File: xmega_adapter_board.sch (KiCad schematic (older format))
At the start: 15 parts, among them J1 Conn_01x04, J2 Conn_01x08, J3 Conn_01x08, J4 Conn_01x04, J5 Conn_01x08, J6 Conn_01x08, J7 Conn_01x08, J8 Conn_01x08, U1 ATxmega256D3-AU

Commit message: Schematic als PDF erstellt
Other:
- note added: "Stützkondensatoren, so dicht wie möglich an U1 platzieren!"
- moved on the sheet: C1, C2, C3, C4, C5, C6, J1, J2, J3, J4, J5, J6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

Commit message: Power LED als rote SMD LED hinzugefuegt
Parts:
- added D1: LED ROT (2,0V / 20mA), LED_SMD:LED_0805_2012Metric_Pad1.15x1.40mm_HandSolder, symbol Device:LED
- added R1: 68, Resistor_SMD:R_0805_2012Metric_Pad1.15x1.40mm_HandSolder, symbol Device:R
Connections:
- net GND: now also D1.1 (K)
- net VCC renamed +3V3
- net +3V3: now also R1.2
- new net: D1.2 (A), R1.1
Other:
- note added: "Spannungsversorgung"
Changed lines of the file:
@@
 Sheet 1 1
 Title "XMEGA Adapter Board "
-Date "2020-06-25"
-Rev "1.0.0"
+Date "2020-07-12"
+Rev "1.1.0"
 Comp ""
 Comment1 "Erstellt von: Thorsten Kattanek"
@@
 Wire Wire Line
 	2900 6300 2900 6500
-Text GLabel 2900 2500 1    50   Input ~ 0
+Text GLabel 700  1250 3    50   Input ~ 0
 VCC
 Text GLabel 3000 2500 1    50   Input ~ 0
@@
 Text Notes 7900 750  0    50   ~ 0
 Stützkondensatoren, so dicht wie möglich an U1 platzieren!
+$Comp
+L Device:LED D1
+U 1 1 5F0B2F15
+P 4300 1350
+F 0 "D1" H 4293 1095 50  0000 C CNN
+F 1 "LED ROT (2,0V / 20mA)" H 4293 1186 50  0000 C CNN
+F 2 "LED_SMD:LED_0805_2012Metric_Pad1.15x1.40mm_HandSolder" H 4300 1350 50  0001 C CNN
+F 3 "~" H 4300 1350 50  0001 C CNN
+	1    4300 1350
+	-1   0    0    1
+$EndComp
+Text GLabel 1100 1250 3    50   Input ~ 0
+GND
+Wire Wire Line
+	4450 1350 4650 1350
+$Comp
+L power:+3.3V #PWR01
+U 1 1 5F0BBD4E
+P 700 1000
+F 0 "#PWR01" H 700 850 50  0001 C CNN
+F 1 "+3.3V" H 715 1173 50  0000 C CNN
+F 2 "" H 700 1000 50  0001 C CNN
+F 3 "" H 700 1000 50  0001 C CNN
+	1    700  1000
+	1    0    0    -1
+$EndComp
+$Comp
+L power:GND #PWR03
+U 1 1 5F0BCF31
+P 1100 1000
+F 0 "#PWR03" H 1100 750 50  0001 C CNN
+F 1 "GND" H 1105 827 50  0000 C CNN
+F 2 "" H 1100 1000 50  0001 C CNN
+F 3 "" H 1100 1000 50  0001 C CNN
+	1    1100 1000
+	-1   0    0    1
+$EndComp
+Wire Wire Line
+	700  1000 700  1250
+Wire Wire Line
+	1100 1000 1100 1250
+Text Notes 600  650  0    50   ~ 0
+Spannungsversorgung
+Text GLabel 4650 1350 2    50   Input ~ 0
+GND
+Text GLabel 3100 1350 0    50   Input ~ 0
+VCC
+$Comp
+L Device:R R1
+U 1 1 5F101B02
+P 3550 1350
+F 0 "R1" V 3343 1350 50  0000 C CNN
+F 1 "68" V 3434 1350 50  0000 C CNN
+F 2 "Resistor_SMD:R_0805_2012Metric_Pad1.15x1.40mm_HandSolder" V 3480 1350 50  0001 C CNN
+F 3 "~" H 3550 1350 50  0001 C CNN
+	1    3550 1350
+	0    1    1    0
+$EndComp
+Wire Wire Line
+	3700 1350 4150 1350
+Wire Wire Line
+	3400 1350 3100 1350
+Text GLabel 2900 2500 1    50   Input ~ 0
+VCC
 $EndSCHEMATC

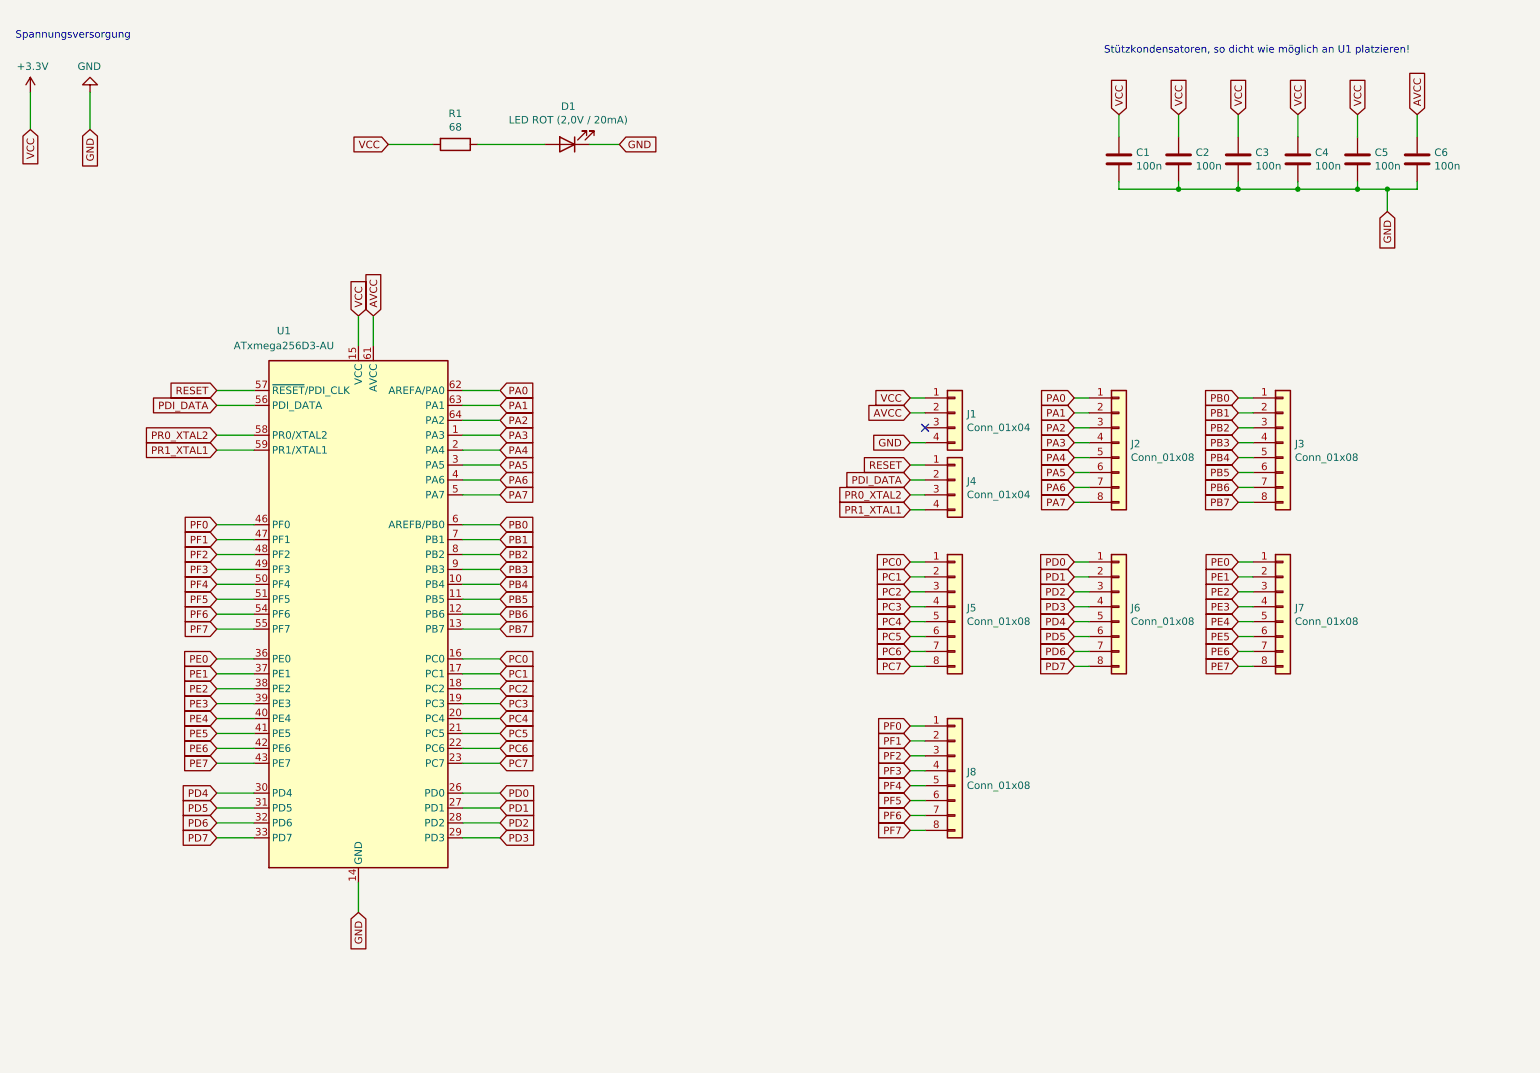
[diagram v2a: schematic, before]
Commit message: changed board to version 1.1.0 - added a 3.3 voltage regulator and a reset button
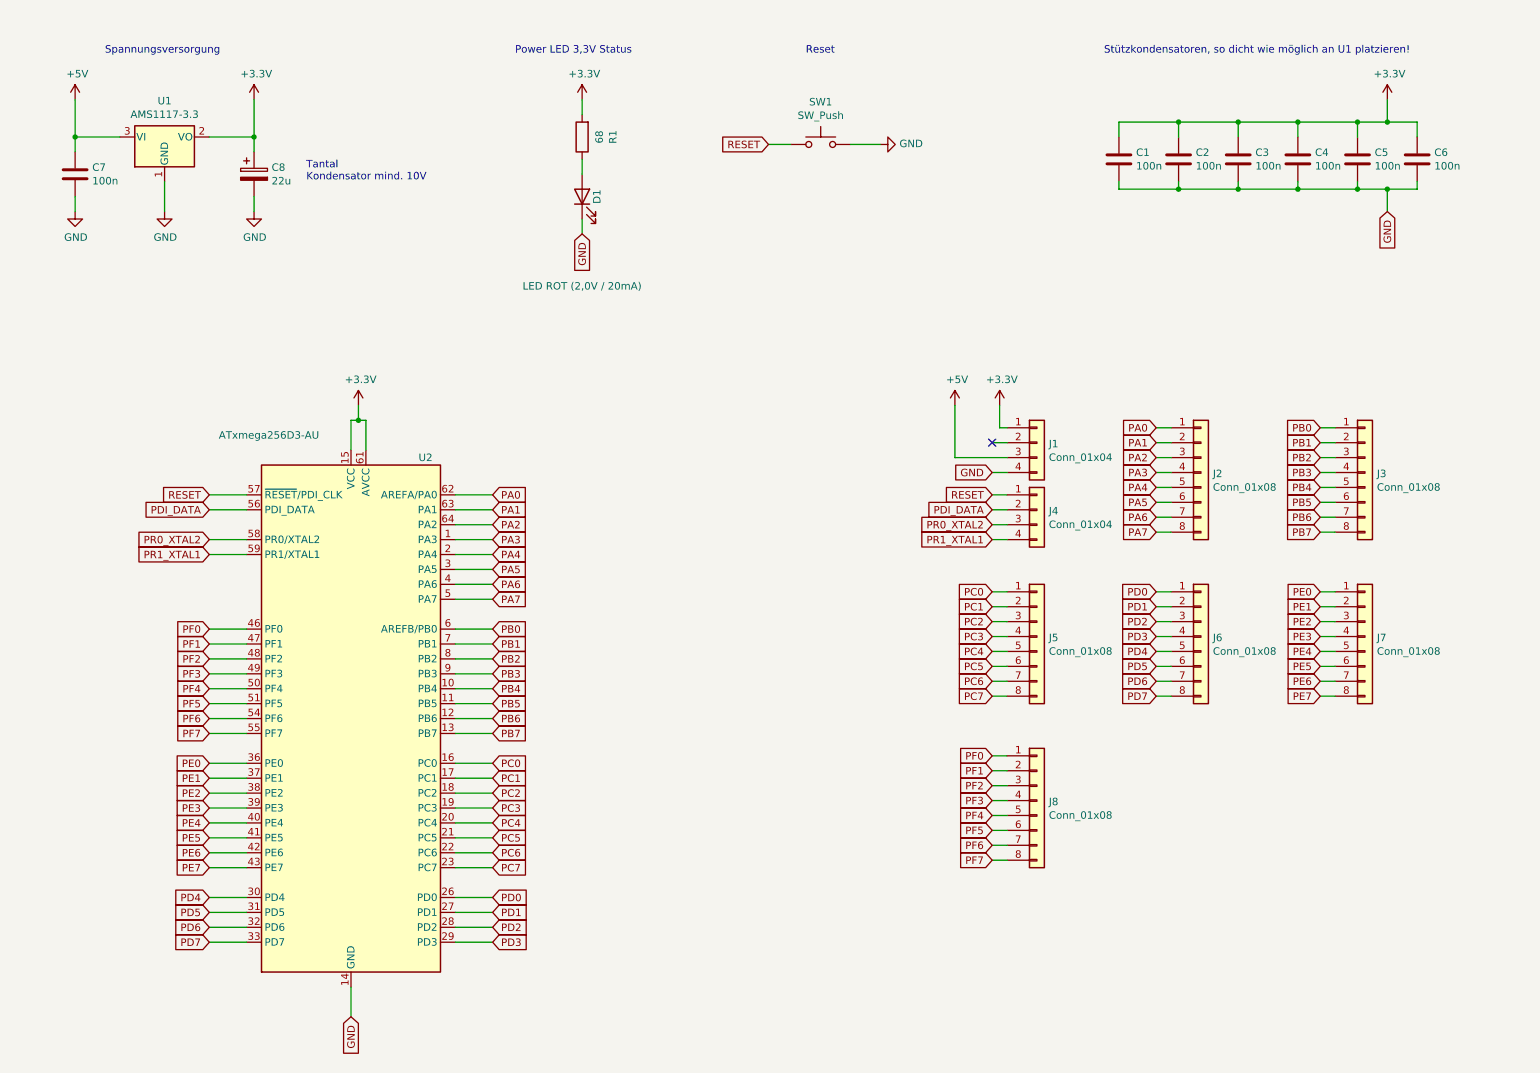
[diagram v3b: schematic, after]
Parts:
- removed U1: ATxmega256D3-AU, Package_QFP:TQFP-64_14x14mm_P0.8mm, symbol MCU_Microchip_ATmega:ATxmega256D3-AU
- added C7: 100n, Capacitor_SMD:C_0805_2012Metric_Pad1.18x1.45mm_HandSolder, symbol Device:C
- added C8: 22u, Capacitor_Tantalum_SMD:CP_EIA-3528-12_Kemet-T_Pad1.50x2.35mm_HandSolder, symbol Device:CP
- added SW1: SW_Push, button_switch_tk:SW_KMR231G, symbol Switch:SW_Push
- added U1: AMS1117-3.3, Package_TO_SOT_SMD:SOT-223-3_TabPin2, symbol Regulator_Linear:AMS1117-3.3
- added U2: ATxmega256D3-AU, Package_QFP:TQFP-64_14x14mm_P0.8mm, symbol MCU_Microchip_ATmega:ATxmega256D3-AU
- C1, C2, C3, C4, C5, C6: footprint Capacitor_SMD:C_0805_2012Metric_Pad1.15x1.40mm_HandSolder -> Capacitor_SMD:C_0805_2012Metric_Pad1.18x1.45mm_HandSolder
- R1: footprint Resistor_SMD:R_0805_2012Metric_Pad1.15x1.40mm_HandSolder -> Resistor_SMD:R_0805_2012Metric_Pad1.20x1.40mm_HandSolder
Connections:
- net +3V3: now also C6.1, C8.1, U1.2 (VO), U2.15 (VCC), U2.25 (VCC), U2.35 (VCC), U2.45 (VCC), U2.53 (VCC), U2.61 (AVCC)
- net GND: now also C7.2, C8.2, SW1.2, U1.1 (GND), U2.14 (GND), U2.24 (GND), U2.34 (GND), U2.44 (GND), U2.52 (GND), U2.60 (GND)
- net PA0: now also U2.62 (AREFA/PA0)
- net PA1: now also U2.63 (PA1)
- net PA2: now also U2.64 (PA2)
- net PA3: now also U2.1 (PA3)
- net PA4: now also U2.2 (PA4)
- net PA5: now also U2.3 (PA5)
- net PA6: now also U2.4 (PA6)
- net PA7: now also U2.5 (PA7)
- net PB0: now also U2.6 (AREFB/PB0)
- net PB1: now also U2.7 (PB1)
- net PB2: now also U2.8 (PB2)
- net PB3: now also U2.9 (PB3)
- net PB4: now also U2.10 (PB4)
- net PB5: now also U2.11 (PB5)
- net PB6: now also U2.12 (PB6)
- net PB7: now also U2.13 (PB7)
- net PC0: now also U2.16 (PC0)
- net PC1: now also U2.17 (PC1)
- net PC2: now also U2.18 (PC2)
- net PC3: now also U2.19 (PC3)
- net PC4: now also U2.20 (PC4)
- net PC5: now also U2.21 (PC5)
- net PC6: now also U2.22 (PC6)
- net PC7: now also U2.23 (PC7)
- net PD0: now also U2.26 (PD0)
- net PD1: now also U2.27 (PD1)
- net PD2: now also U2.28 (PD2)
- net PD3: now also U2.29 (PD3)
- net PD4: now also U2.30 (PD4)
- net PD5: now also U2.31 (PD5)
- net PD6: now also U2.32 (PD6)
- net PD7: now also U2.33 (PD7)
- net PDI_DATA: now also U2.56 (PDI_DATA)
- net PE0: now also U2.36 (PE0)
- net PE1: now also U2.37 (PE1)
- net PE2: now also U2.38 (PE2)
- net PE3: now also U2.39 (PE3)
- net PE4: now also U2.40 (PE4)
- net PE5: now also U2.41 (PE5)
- net PE6: now also U2.42 (PE6)
- net PE7: now also U2.43 (PE7)
- net PF0: now also U2.46 (PF0)
- net PF1: now also U2.47 (PF1)
- net PF2: now also U2.48 (PF2)
- net PF3: now also U2.49 (PF3)
- net PF4: now also U2.50 (PF4)
- net PF5: now also U2.51 (PF5)
- net PF6: now also U2.54 (PF6)
- net PF7: now also U2.55 (PF7)
- net PR0_XTAL2: now also U2.58 (PR0/XTAL2)
- net PR1_XTAL1: now also U2.59 (PR1/XTAL1)
- net RESET: now also SW1.1, U2.57 (~RESET~/PDI_CLK)
- net +5V: now reaches J1.3 (Pin_3)
- net +5V: now also C7.1, U1.3 (VI)
- net AVCC: no longer names the net of J1.2 (Pin_2)
- net AVCC: no longer C6.1
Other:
- note added: "Power LED 3,3V Status"
- note added: "Reset\n"
- note added: "Tantal\nKondensator mind. 10V"
- moved on the sheet: D1, J1, J2, J3, J4, J5, J6, J7, J8, R1
